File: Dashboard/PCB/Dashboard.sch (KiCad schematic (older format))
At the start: 96 parts, among them J1 Display, J2 Conn_01x26_Female, J3 LED, J7 PROGRAMMER, SW1 SW_SPST, U1 STM32F767ZIT6, U10 24LC01, U2 MP2359DJ-LF-Z, U3 MP2359DJ-LF-Z, U4 AS4C1M16S-6TCN, U5 AT25SF128A-SHB-T, U6 MP2332H, U7 MCP2561-E-SN, U8 MCP2561-E-SN, U9 ESP-12S, Y1 Crystal_GND24

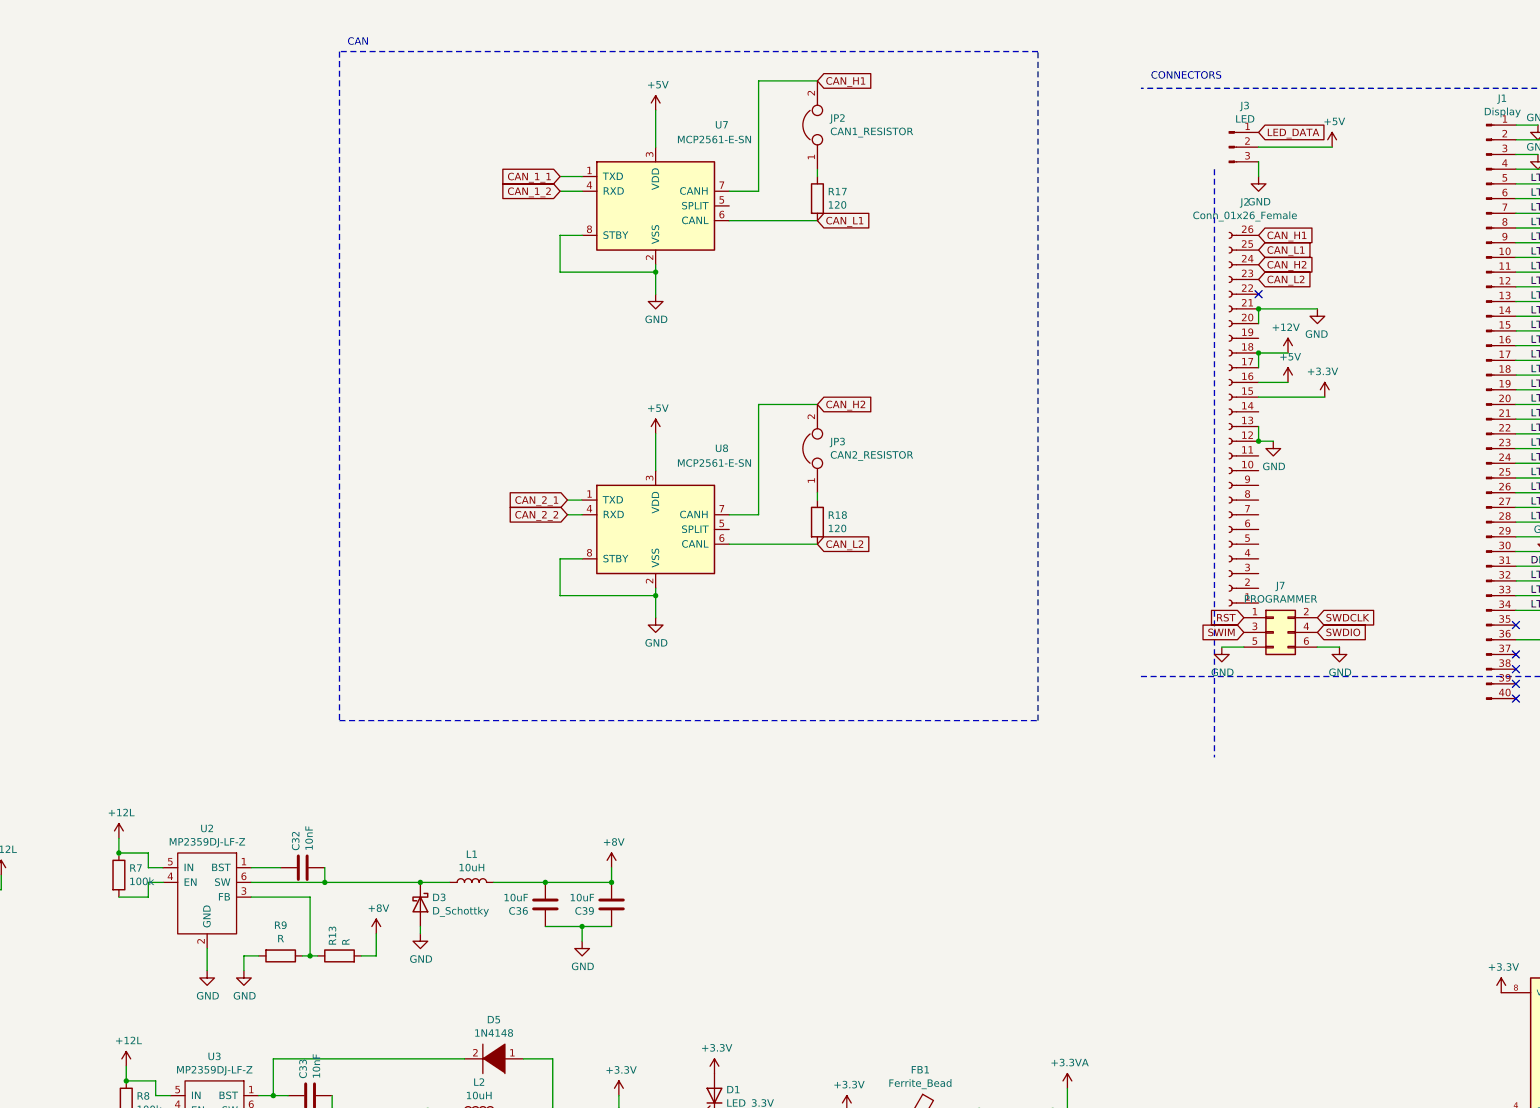
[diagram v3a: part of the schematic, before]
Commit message: New pcb board
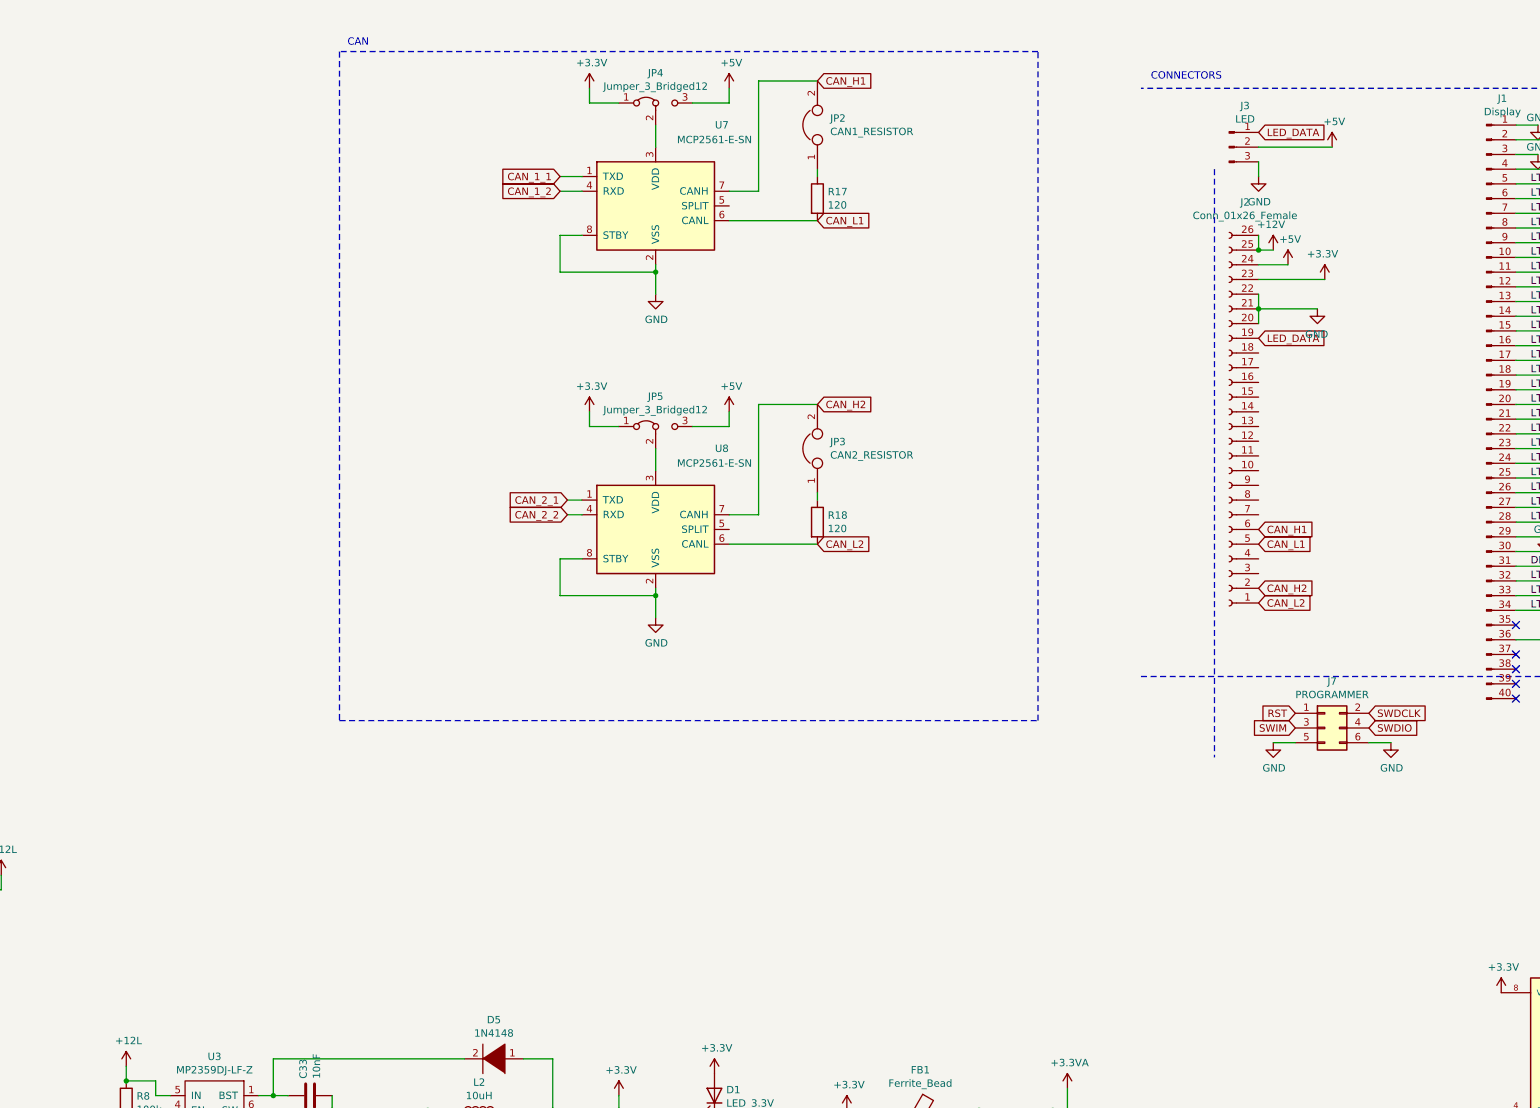
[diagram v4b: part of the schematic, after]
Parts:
- removed C32: 10nF, Capacitor_SMD:C_0805_2012Metric, symbol Device:C
- removed C36, C39: 10uF, Capacitor_SMD:C_0805_2012Metric, symbol Device:C
- removed D3: D_Schottky, Diode_SMD:D_0805_2012Metric, symbol Device:D_Schottky
- removed L1: 10uH, Inductor_SMD:L_Vishay_IHLP-1616, symbol Device:L
- removed R13, R9: R, Resistor_SMD:R_0805_2012Metric, symbol Device:R
- removed R7: 100k, Resistor_SMD:R_0805_2012Metric, symbol Device:R
- removed U2: MP2359DJ-LF-Z, Package_SO:SOIC-8-1EP_3.9x4.9mm_P1.27mm_EP2.29x3mm, symbol Regulator_Controller:MP2359DJ-LF-Z
- added JP4, JP5: Jumper_3_Bridged12, Jumper:SolderJumper-3_P1.3mm_Open_Pad1.0x1.5mm, symbol Jumper:Jumper_3_Bridged12
- U7, U8: footprint Package_SO:SOIC-8_3.9x4.9mm_P1.27mm -> Package_DIP:DIP-8_W7.62mm
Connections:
- net +12V: now also J2.25 (Pin_25), J2.26 (Pin_26); no longer J2.17 (Pin_17), J2.18 (Pin_18)
- net +3V3: now also J2.23 (Pin_23), JP4.1 (A), JP5.1 (A); no longer J2.15 (Pin_15)
- net +5V: now also J2.24 (Pin_24), JP4.3 (B), JP5.3 (B); no longer J2.16 (Pin_16), U7.3 (VDD), U8.3 (VDD)
- net CAN_H1: now also J2.6 (Pin_6); no longer J2.26 (Pin_26)
- net CAN_H2: now also J2.2 (Pin_2); no longer J2.24 (Pin_24)
- net CAN_L1: now also J2.5 (Pin_5); no longer J2.25 (Pin_25)
- net CAN_L2: now also J2.1 (Pin_1); no longer J2.23 (Pin_23)
- net GND: now also J2.22 (Pin_22); no longer J2.12 (Pin_12), J2.13 (Pin_13)
- net LED_DATA: now also J2.19 (Pin_19)
- new net: JP5.2 (C), U8.3 (VDD)
- new net: JP4.2 (C), U7.3 (VDD)
- no-connect marks 47 -> 46
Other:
- moved on the sheet: J7

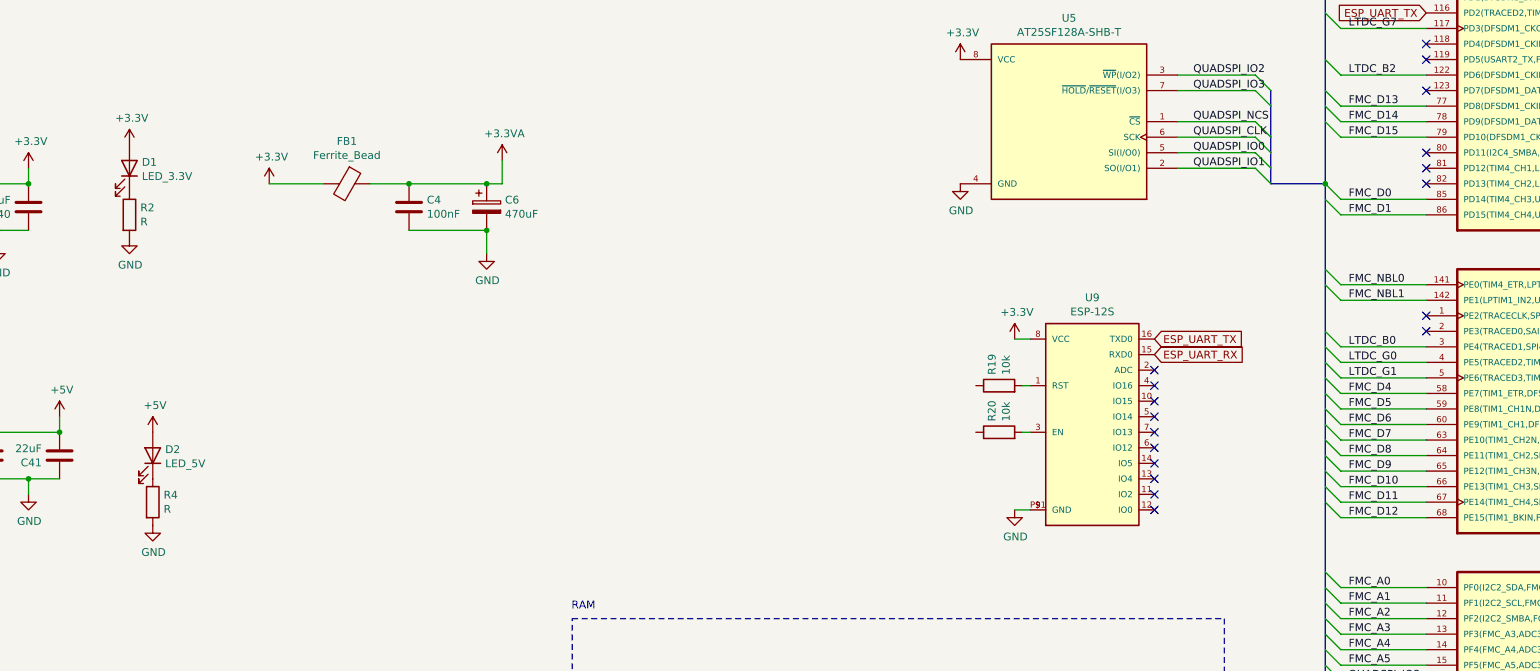
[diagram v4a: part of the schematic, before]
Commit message: Add signal led
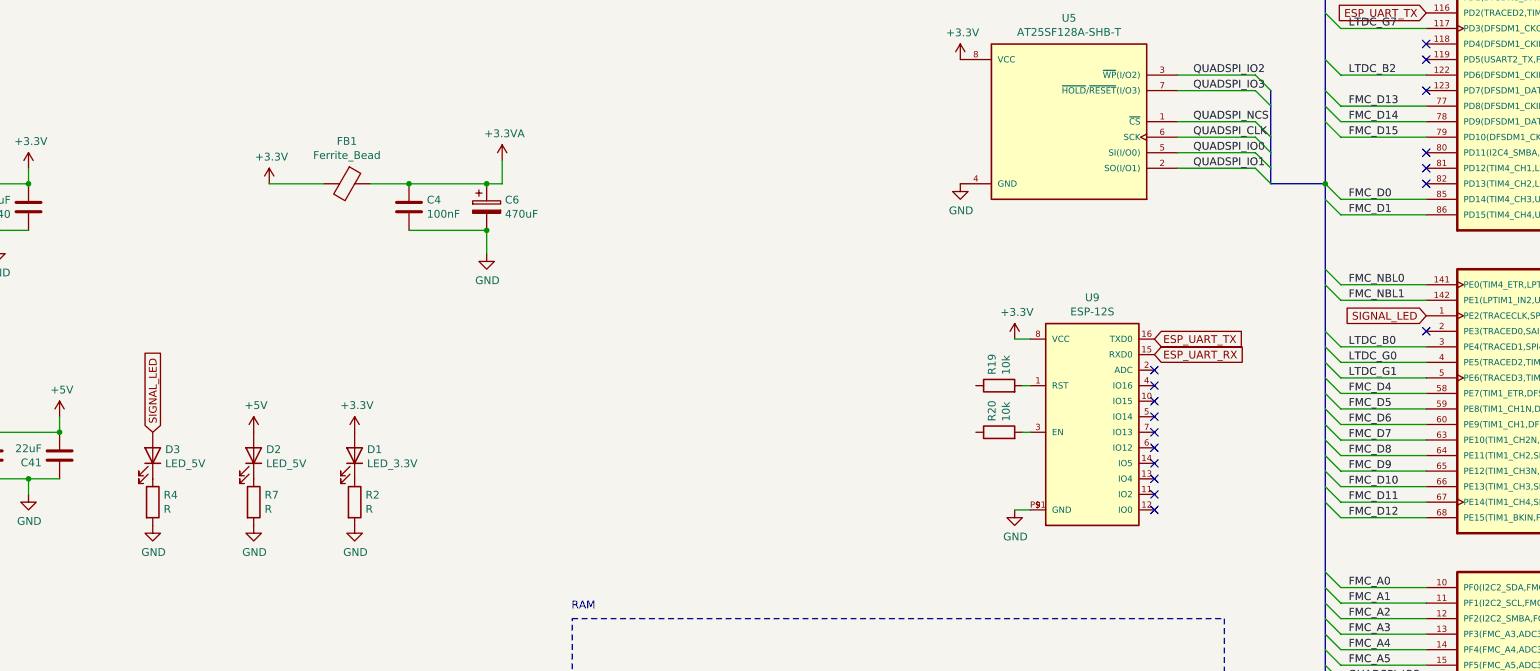
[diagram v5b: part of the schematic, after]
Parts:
- added D3: LED_5V, LED_SMD:LED_0805_2012Metric, symbol Device:LED
- added R7: R, Resistor_SMD:R_0805_2012Metric, symbol Device:R
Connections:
- net GND: now also R7.2
- net SIGNAL_LED: now reaches U1.1 (PE2(TRACECLK,SP14_SCK,SAI1_MCLK_A,QUADSPI_BK1_IO2,ETH_MII_TXD3,FMC_A23))
- net SIGNAL_LED: now also D3.2 (A)
- net at D2.1 (K): now also R7.1; no longer R4.1
- new net: D3.1 (K), R4.1
- no-connect marks 46 -> 45
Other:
- moved on the sheet: D1, D2, R2
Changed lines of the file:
@@
 	1    0    0    -1
 $EndComp
-$Comp
-L STM32F767ZIT6:STM32F767ZIT6 U1
-U 6 1 617AB936
-P 17600 9300
-F 0 "U1" H 19833 9296 50  0000 L CNN
-F 1 "STM32F767ZIT6" H 19833 9205 50  0000 L CNN
-F 2 "STM32F767ZIT6:QFP50P2200X2200X160-144N" H 17600 9300 50  0001 L BNN
-F 3 "" H 17600 9300 50  0001 L BNN
-F 4 "6" H 17600 9300 50  0001 L BNN "PARTREV"
-F 5 "STMicroelectronics" H 17600 9300 50  0001 L BNN "MF"
-F 6 "LQFP-144 STMicroelectronics" H 17600 9300 50  0001 L BNN "PACKAGE"
-F 7 "IPC-7351B" H 17600 9300 50  0001 L BNN "STANDARD"
-F 8 "IC MCU 32BIT 2MB FLASH 144LQFP" H 17600 9300 50  0001 L BNN "DESCRIPTION"
-F 9 "STM32F767ZIT6" H 17600 9300 50  0001 L BNN "MP"
-F 10 "14.84 USD" H 17600 9300 50  0001 L BNN "PRICE"
-F 11 "Good" H 17600 9300 50  0001 L BNN "AVAILABILITY"
-	6    17600 9300
-	1    0    0    -1
-$EndComp
 Text Label 14700 11650 0    50   ~ 0
 FMC_SDNRAS
@@
 NoConn ~ 15200 7850
 NoConn ~ 15200 7950
-NoConn ~ 15200 8800
 NoConn ~ 15200 8900
 NoConn ~ 15200 12600
@@
 L Device:LED D2
 U 1 1 621EB984
-P 7000 9700
-F 0 "D2" V 7039 9780 50  0000 L CNN
-F 1 "LED_5V" V 6948 9780 50  0000 L CNN
-F 2 "LED_SMD:LED_0805_2012Metric" H 7000 9700 50  0001 C CNN
-F 3 "~" H 7000 9700 50  0001 C CNN
-	1    7000 9700
+P 7650 9700
+F 0 "D2" V 7689 9780 50  0000 L CNN
+F 1 "LED_5V" V 7598 9780 50  0000 L CNN
+F 2 "LED_SMD:LED_0805_2012Metric" H 7650 9700 50  0001 C CNN
+F 3 "~" H 7650 9700 50  0001 C CNN
+	1    7650 9700
 	0    1    -1   0
 $EndComp
@@
 L power:GND #PWR014
 U 1 1 621D9EE0
-P 6850 8300
-F 0 "#PWR014" H 6850 8050 50  0001 C CNN
-F 1 "GND" H 6855 8127 50  0000 C CNN
-F 2 "" H 6850 8300 50  0001 C CNN
-F 3 "" H 6850 8300 50  0001 C CNN
-	1    6850 8300
+P 8300 10150
+F 0 "#PWR014" H 8300 9900 50  0001 C CNN
+F 1 "GND" H 8305 9977 50  0000 C CNN
+F 2 "" H 8300 10150 50  0001 C CNN
+F 3 "" H 8300 10150 50  0001 C CNN
+	1    8300 10150
 	1    0    0    -1
 $EndComp
@@
 L power:+3.3V #PWR013
 U 1 1 621CB099
-P 6850 7700
-F 0 "#PWR013" H 6850 7550 50  0001 C CNN
-F 1 "+3.3V" H 6865 7873 50  0000 C CNN
-F 2 "" H 6850 7700 50  0001 C CNN
-F 3 "" H 6850 7700 50  0001 C CNN
-	1    6850 7700
+P 8300 9550
+F 0 "#PWR013" H 8300 9400 50  0001 C CNN
+F 1 "+3.3V" H 8315 9723 50  0000 C CNN
+F 2 "" H 8300 9550 50  0001 C CNN
+F 3 "" H 8300 9550 50  0001 C CNN
+	1    8300 9550
 	1    0    0    -1
 $EndComp
@@
 L Device:R R2
 U 1 1 621CA7FF
-P 6850 8150
-F 0 "R2" H 6920 8196 50  0000 L CNN
-F 1 "R" H 6920 8105 50  0000 L CNN
-F 2 "Resistor_SMD:R_0805_2012Metric" V 6780 8150 50  0001 C CNN
-F 3 "~" H 6850 8150 50  0001 C CNN
-	1    6850 8150
+P 8300 10000
+F 0 "R2" H 8370 10046 50  0000 L CNN
+F 1 "R" H 8370 9955 50  0000 L CNN
+F 2 "Resistor_SMD:R_0805_2012Metric" V 8230 10000 50  0001 C CNN
+F 3 "~" H 8300 10000 50  0001 C CNN
+	1    8300 10000
 	1    0    0    -1
 $EndComp
@@
 L Device:LED D1
 U 1 1 621B492A
-P 6850 7850
-F 0 "D1" V 6889 7930 50  0000 L CNN
-F 1 "LED_3.3V" V 6798 7930 50  0000 L CNN
-F 2 "LED_SMD:LED_0805_2012Metric" H 6850 7850 50  0001 C CNN
-F 3 "~" H 6850 7850 50  0001 C CNN
-	1    6850 7850
+P 8300 9700
+F 0 "D1" V 8339 9780 50  0000 L CNN
+F 1 "LED_3.3V" V 8248 9780 50  0000 L CNN
+F 2 "LED_SMD:LED_0805_2012Metric" H 8300 9700 50  0001 C CNN
+F 3 "~" H 8300 9700 50  0001 C CNN
+	1    8300 9700
 	0    1    -1   0
 $EndComp
 $Comp
-L power:+5V #PWR0127
-U 1 1 62D3D3FD
-P 7000 9550
-F 0 "#PWR0127" H 7000 9400 50  0001 C CNN
-F 1 "+5V" H 7015 9723 50  0000 C CNN
-F 2 "" H 7000 9550 50  0001 C CNN
-F 3 "" H 7000 9550 50  0001 C CNN
-	1    7000 9550
-	1    0    0    -1
-$EndComp
-$Comp
 L ESP-12S:ESP-12S U9
 U 1 1 61B531D3
@@
 Wire Wire Line
 	6450 3600 6450 3450
+$Comp
+L STM32F767ZIT6:STM32F767ZIT6 U1
+U 6 1 617AB936
+P 17600 9300
+F 0 "U1" H 19833 9296 50  0000 L CNN
+F 1 "STM32F767ZIT6" H 19833 9205 50  0000 L CNN
+F 2 "STM32F767ZIT6:QFP50P2200X2200X160-144N" H 17600 9300 50  0001 L BNN
+F 3 "" H 17600 9300 50  0001 L BNN
+F 4 "6" H 17600 9300 50  0001 L BNN "PARTREV"
+F 5 "STMicroelectronics" H 17600 9300 50  0001 L BNN "MF"
+F 6 "LQFP-144 STMicroelectronics" H 17600 9300 50  0001 L BNN "PACKAGE"
+F 7 "IPC-7351B" H 17600 9300 50  0001 L BNN "STANDARD"
+F 8 "IC MCU 32BIT 2MB FLASH 144LQFP" H 17600 9300 50  0001 L BNN "DESCRIPTION"
+F 9 "STM32F767ZIT6" H 17600 9300 50  0001 L BNN "MP"
+F 10 "14.84 USD" H 17600 9300 50  0001 L BNN "PRICE"
+F 11 "Good" H 17600 9300 50  0001 L BNN "AVAILABILITY"
+	6    17600 9300
+	1    0    0    -1
+$EndComp
+Text GLabel 15200 8800 0    50   Input ~ 0
+SIGNAL_LED
+$Comp
+L Device:R R7
+U 1 1 63BD9F88
+P 7650 10000
+F 0 "R7" H 7720 10046 50  0000 L CNN
+F 1 "R" H 7720 9955 50  0000 L CNN
+F 2 "Resistor_SMD:R_0805_2012Metric" V 7580 10000 50  0001 C CNN
+F 3 "~" H 7650 10000 50  0001 C CNN
+	1    7650 10000
+	1    0    0    -1
+$EndComp
+$Comp
+L power:GND #PWR0115
+U 1 1 63BD9F8E
+P 7650 10150
+F 0 "#PWR0115" H 7650 9900 50  0001 C CNN
+F 1 "GND" H 7655 9977 50  0000 C CNN
+F 2 "" H 7650 10150 50  0001 C CNN
+F 3 "" H 7650 10150 50  0001 C CNN
+	1    7650 10150
+	1    0    0    -1
+$EndComp
+$Comp
+L Device:LED D3
+U 1 1 63BD9F94
+P 7000 9700
+F 0 "D3" V 7039 9780 50  0000 L CNN
+F 1 "LED_5V" V 6948 9780 50  0000 L CNN
+F 2 "LED_SMD:LED_0805_2012Metric" H 7000 9700 50  0001 C CNN
+F 3 "~" H 7000 9700 50  0001 C CNN
+	1    7000 9700
+	0    1    -1   0
+$EndComp
+$Comp
+L power:+5V #PWR0116
+U 1 1 63BD9F9A
+P 7650 9550
+F 0 "#PWR0116" H 7650 9400 50  0001 C CNN
+F 1 "+5V" H 7665 9723 50  0000 C CNN
+F 2 "" H 7650 9550 50  0001 C CNN
+F 3 "" H 7650 9550 50  0001 C CNN
+	1    7650 9550
+	1    0    0    -1
+$EndComp
 Wire Bus Line
 	14050 6050 14050 6400
@@
 Wire Bus Line
 	14550 7950 14550 14000
+Text GLabel 7000 9550 1    50   Input ~ 0
+SIGNAL_LED
 $EndSCHEMATC
